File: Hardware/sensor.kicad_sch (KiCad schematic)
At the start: 13 parts

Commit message: Version 0.1
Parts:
- removed TP52: TestPoint_Small, TestPoint:TestPoint_Pad_D1.0mm, symbol Connector:TestPoint_Small
- C1: footprint Capacitor_SMD:C_0805_2012Metric_Pad1.18x1.45mm_HandSolder -> (none)
- C2, C3, C4, C5: footprint Capacitor_SMD:C_0805_2012Metric_Pad1.18x1.45mm_HandSolder -> Capacitor_SMD:C_0603_1608Metric_Pad1.08x0.95mm_HandSolder
- R1, R2, R3, R4: footprint Resistor_SMD:R_0805_2012Metric_Pad1.20x1.40mm_HandSolder -> Resistor_SMD:R_0603_1608Metric_Pad0.98x0.95mm_HandSolder
- U1: value (none) -> OPA2376xxD
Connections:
- net +5V renamed +3V3
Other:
- moved on the sheet: U1A, U1B, U1C

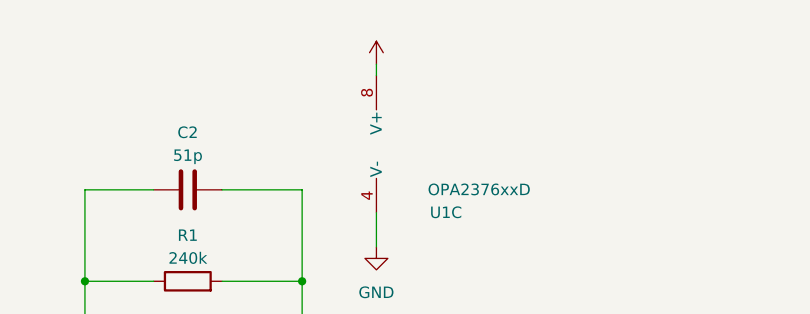
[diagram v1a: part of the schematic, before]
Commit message: Readme + hole update
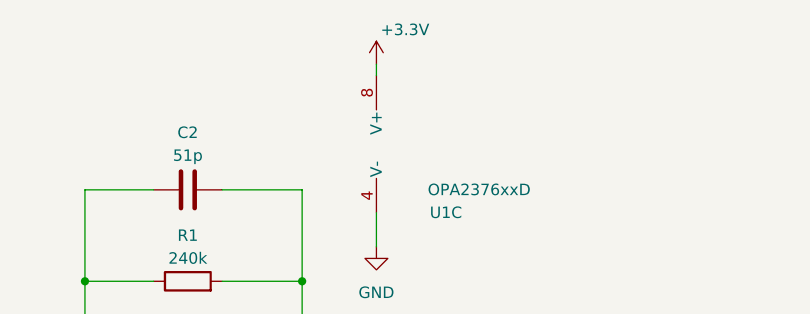
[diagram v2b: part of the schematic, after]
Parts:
- C1: footprint (none) -> Capacitor_SMD:C_0603_1608Metric_Pad1.08x0.95mm_HandSolder
- U1: footprint (none) -> OPA2376AID:SOIC127P599X175-8N
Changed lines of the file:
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@@
       (effects (font (size 1.27 1.27)) (justify right))
     )
-    (property "Footprint" "" (id 2) (at 154.94 58.42 0)
+    (property "Footprint" "OPA2376AID:SOIC127P599X175-8N" (id 2) (at 154.94 58.42 0)
       (effects (font (size 1.27 1.27)) hide)
     )
@@
     (property "Reference" "U1" (id 0) (at 132.715 87.63 0))
     (property "Value" "OPA2376xxD" (id 1) (at 136.525 85.09 0))
-    (property "Footprint" "" (id 2) (at 130.81 92.71 0)
+    (property "Footprint" "OPA2376AID:SOIC127P599X175-8N" (id 2) (at 130.81 92.71 0)
       (effects (font (size 1.27 1.27)) hide)
     )
@@
       (effects (font (size 1.27 1.27)) hide)
     )
-    (property "Value" "" (id 1) (at 155.575 45.72 0))
+    (property "Value" "+3.3V" (id 1) (at 155.575 45.72 0))
     (property "Footprint" "" (id 2) (at 152.4 49.53 0)
       (effects (font (size 1.27 1.27)) hide)
@@
     (property "Reference" "U1" (id 0) (at 130.81 115.57 0))
     (property "Value" "OPA2376xxD" (id 1) (at 130.81 113.03 0))
-    (property "Footprint" "" (id 2) (at 130.81 105.41 0)
+    (property "Footprint" "OPA2376AID:SOIC127P599X175-8N" (id 2) (at 130.81 105.41 0)
       (effects (font (size 1.27 1.27)) hide)
     )
@@
       (effects (font (size 1.27 1.27)) (justify right))
     )
-    (property "Footprint" "" (id 2) (at 103.2002 109.22 0)
+    (property "Footprint" "Capacitor_SMD:C_0603_1608Metric_Pad1.08x0.95mm_HandSolder" (id 2) (at 103.2002 109.22 0)
       (effects (font (size 1.27 1.27)) hide)
     )

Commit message: Updated power design
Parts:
- U1: value OPA2376xxD -> (none); footprint OPA2376AID:SOIC127P599X175-8N -> (none)
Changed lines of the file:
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@@
       (effects (font (size 1.27 1.27)) (justify right))
     )
-    (property "Value" "OPA2376xxD" (id 1) (at 169.545 63.5 0)
+    (property "Value" "" (id 1) (at 169.545 63.5 0)
       (effects (font (size 1.27 1.27)) (justify right))
     )
-    (property "Footprint" "OPA2376AID:SOIC127P599X175-8N" (id 2) (at 154.94 58.42 0)
+    (property "Footprint" "" (id 2) (at 154.94 58.42 0)
       (effects (font (size 1.27 1.27)) hide)
     )
@@
     (in_bom yes) (on_board yes)
     (property "Reference" "U1" (id 0) (at 132.715 87.63 0))
-    (property "Value" "OPA2376xxD" (id 1) (at 136.525 85.09 0))
-    (property "Footprint" "OPA2376AID:SOIC127P599X175-8N" (id 2) (at 130.81 92.71 0)
+    (property "Value" "" (id 1) (at 136.525 85.09 0))
+    (property "Footprint" "" (id 2) (at 130.81 92.71 0)
       (effects (font (size 1.27 1.27)) hide)
     )
@@
     (in_bom yes) (on_board yes)
     (property "Reference" "U1" (id 0) (at 130.81 115.57 0))
-    (property "Value" "OPA2376xxD" (id 1) (at 130.81 113.03 0))
-    (property "Footprint" "OPA2376AID:SOIC127P599X175-8N" (id 2) (at 130.81 105.41 0)
+    (property "Value" "" (id 1) (at 130.81 113.03 0))
+    (property "Footprint" "" (id 2) (at 130.81 105.41 0)
       (effects (font (size 1.27 1.27)) hide)
     )

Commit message: Updated from discord feedback
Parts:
- U1: value (none) -> OPA2376xxD; footprint (none) -> OPA2376AID:SOIC127P599X175-8N
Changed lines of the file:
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@@
       (effects (font (size 1.27 1.27)) (justify right))
     )
-    (property "Value" "" (id 1) (at 169.545 63.5 0)
+    (property "Value" "OPA2376xxD" (id 1) (at 169.545 63.5 0)
       (effects (font (size 1.27 1.27)) (justify right))
     )
-    (property "Footprint" "" (id 2) (at 154.94 58.42 0)
+    (property "Footprint" "OPA2376AID:SOIC127P599X175-8N" (id 2) (at 154.94 58.42 0)
       (effects (font (size 1.27 1.27)) hide)
     )
@@
     (in_bom yes) (on_board yes)
     (property "Reference" "U1" (id 0) (at 132.715 87.63 0))
-    (property "Value" "" (id 1) (at 136.525 85.09 0))
-    (property "Footprint" "" (id 2) (at 130.81 92.71 0)
+    (property "Value" "OPA2376xxD" (id 1) (at 136.525 85.09 0))
+    (property "Footprint" "OPA2376AID:SOIC127P599X175-8N" (id 2) (at 130.81 92.71 0)
       (effects (font (size 1.27 1.27)) hide)
     )
@@
     (in_bom yes) (on_board yes)
     (property "Reference" "U1" (id 0) (at 130.81 115.57 0))
-    (property "Value" "" (id 1) (at 130.81 113.03 0))
-    (property "Footprint" "" (id 2) (at 130.81 105.41 0)
+    (property "Value" "OPA2376xxD" (id 1) (at 130.81 113.03 0))
+    (property "Footprint" "OPA2376AID:SOIC127P599X175-8N" (id 2) (at 130.81 105.41 0)
       (effects (font (size 1.27 1.27)) hide)
     )

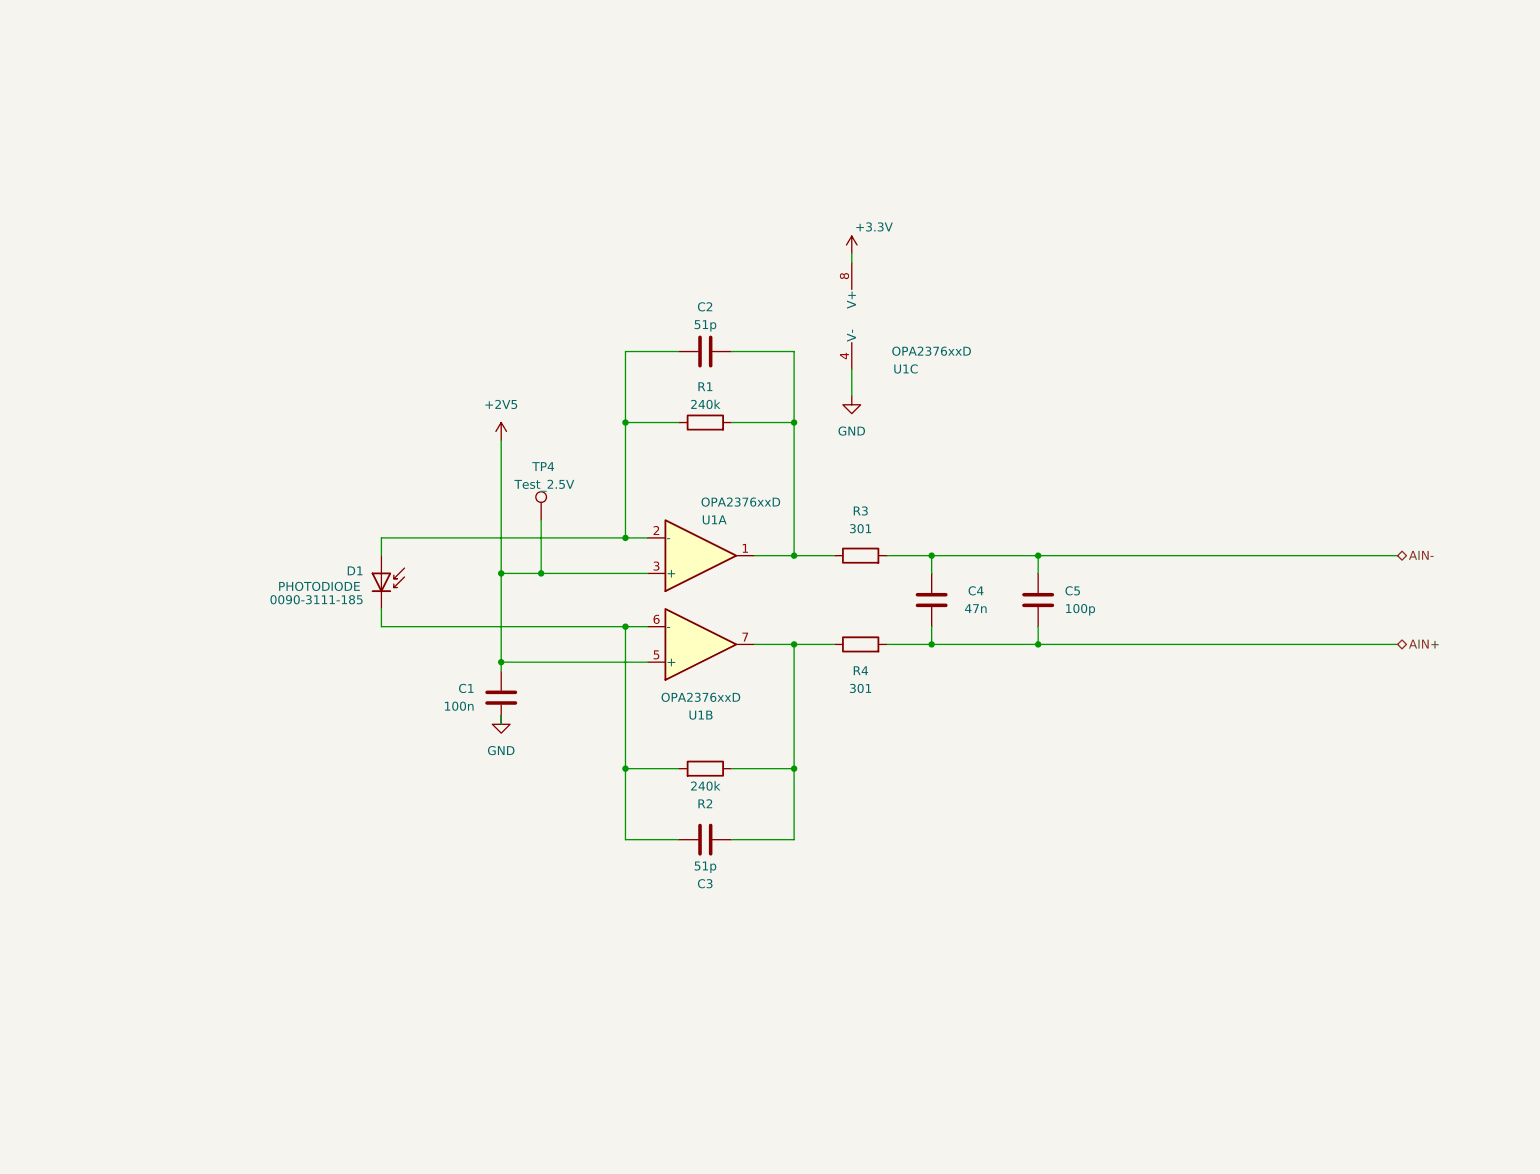
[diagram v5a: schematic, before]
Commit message: initial branch commit with rought layout changes
Signed-off-by: Lawrence Kincheloe <lawrence.kincheloe@mavericktechok.com>
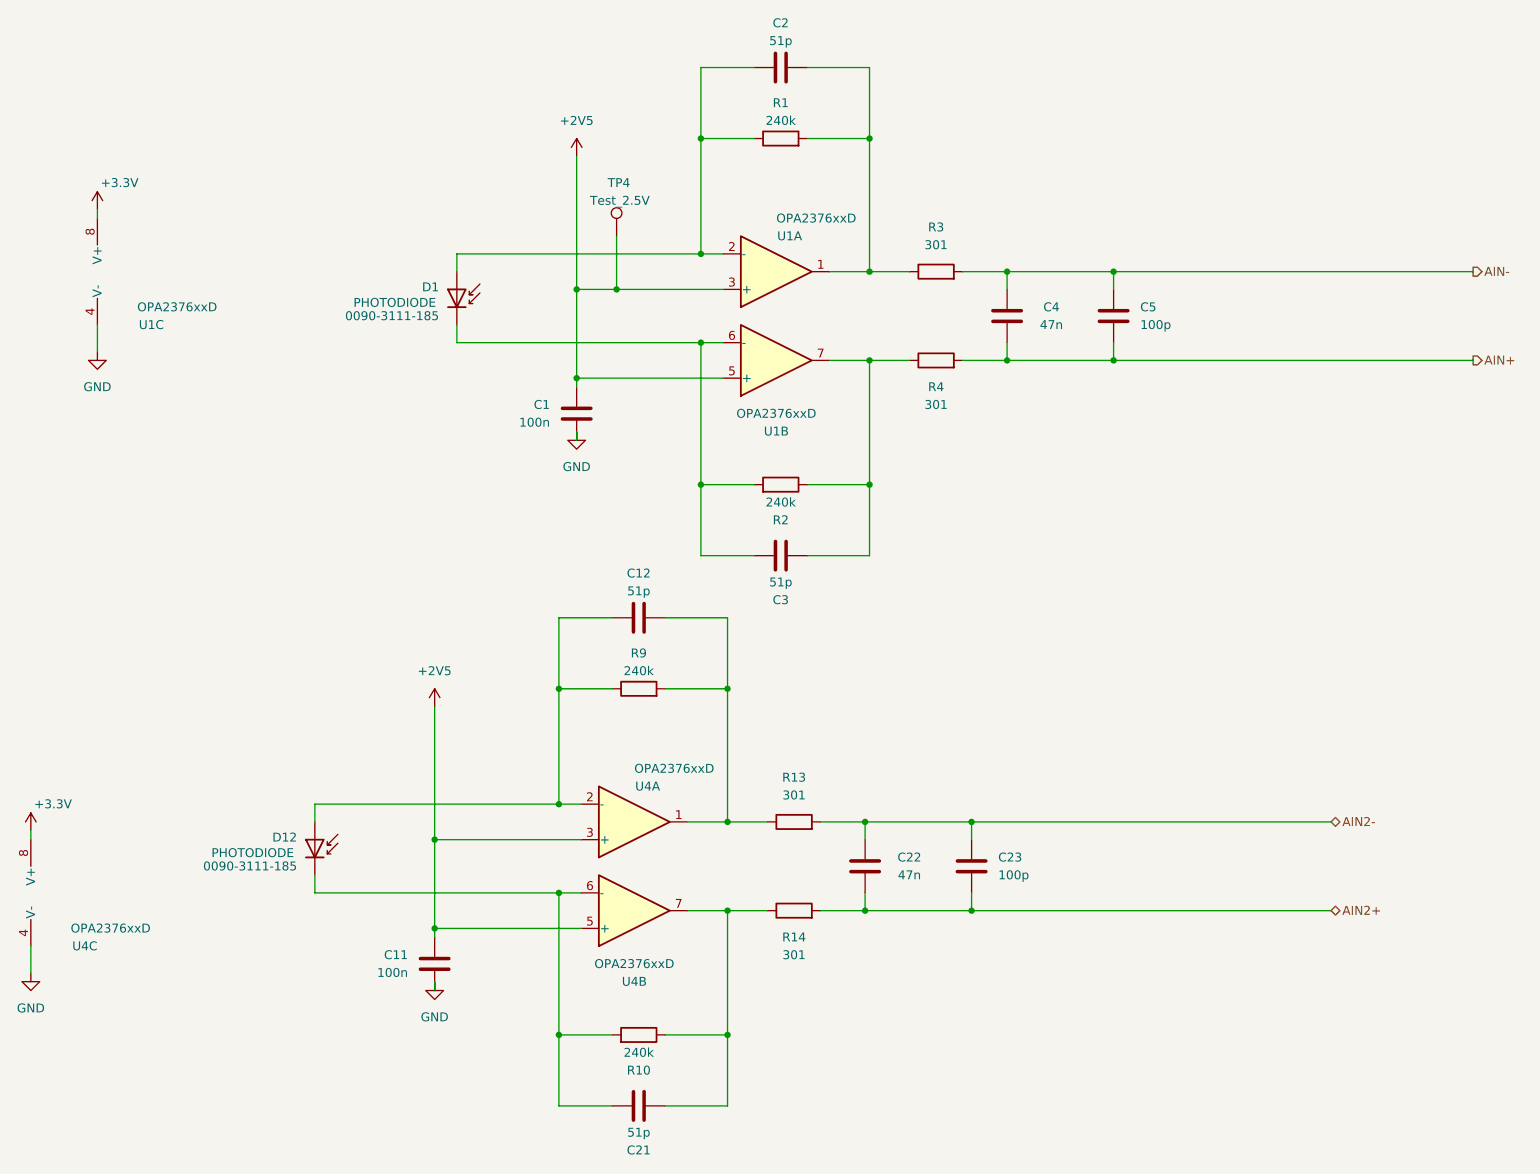
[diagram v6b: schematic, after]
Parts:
- added C11: 100n, Capacitor_SMD:C_0603_1608Metric_Pad1.08x0.95mm_HandSolder, symbol Device:C
- added C12, C21: 51p, Capacitor_SMD:C_0603_1608Metric_Pad1.08x0.95mm_HandSolder, symbol Device:C
- added C22: 47n, Capacitor_SMD:C_0603_1608Metric_Pad1.08x0.95mm_HandSolder, symbol Device:C
- added C23: 100p, Capacitor_SMD:C_0603_1608Metric_Pad1.08x0.95mm_HandSolder, symbol Device:C
- added D12: 0090-3111-185, Diode_SMD:D_1206_3216Metric_Pad1.42x1.75mm_HandSolder, symbol Device:D_Photo
- added R10, R9: 240k, Resistor_SMD:R_0603_1608Metric_Pad0.98x0.95mm_HandSolder, symbol Device:R
- added R13, R14: 301, Resistor_SMD:R_0603_1608Metric_Pad0.98x0.95mm_HandSolder, symbol Device:R
- added U4: OPA2376xxD, OPA2376AID:SOIC127P599X175-8N, symbol Amplifier_Operational:OPA2376xxD
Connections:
- net +2V5: now also C11.2, U4.3 (+), U4.5 (+)
- net +3V3: now also U4.8 (V+)
- net GND: now also C11.1, U4.4 (V-)
- new net: C12.2, R13.1, R9.2, U4.1
- new net: C12.1, D12.2 (A), R9.1, U4.2 (-)
- new net: C21.1, D12.1 (K), R10.2, U4.6 (-)
- new net: C21.2, R10.1, R14.1, U4.7
- new net AIN2+: C22.1, C23.2, R14.2
- new net AIN2-: C22.2, C23.1, R13.2
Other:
- moved on the sheet: C1, C2, C3, C4, C5, D1, R1, R2, R3, R4, TP4, U1A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
